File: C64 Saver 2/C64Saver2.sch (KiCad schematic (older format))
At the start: 20 parts, among them J1 Conn_01x04, J2 Conn_01x08, J4 Conn_01x08, J5 Conn_01x04, J6 Conn_01x04, Q1 2N7002, Q2 Q_PMOS_GDS

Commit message: resistor values
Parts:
- R1, R6: value R -> 3k9
- R2, R3: value R -> 3k3
- R4: value R -> 330k
- R5: value R -> 33k
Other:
- moved on the sheet: R1, R3
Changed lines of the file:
@@
 L R R1
 U 1 1 5AFB3CB5
-P 3650 3050
-F 0 "R1" V 3730 3050 50  0000 C CNN
-F 1 "R" V 3650 3050 50  0000 C CNN
-F 2 "Resistors_THT:R_Axial_DIN0204_L3.6mm_D1.6mm_P5.08mm_Horizontal" V 3580 3050 50  0001 C CNN
-F 3 "" H 3650 3050 50  0001 C CNN
-	1    3650 3050
+P 3650 3150
+F 0 "R1" V 3730 3150 50  0000 C CNN
+F 1 "3k9" V 3650 3150 50  0000 C CNN
+F 2 "Resistors_THT:R_Axial_DIN0204_L3.6mm_D1.6mm_P5.08mm_Horizontal" V 3580 3150 50  0001 C CNN
+F 3 "" H 3650 3150 50  0001 C CNN
+	1    3650 3150
 	1    0    0    -1
 $EndComp
@@
 P 3650 4300
 F 0 "R2" V 3730 4300 50  0000 C CNN
-F 1 "R" V 3650 4300 50  0000 C CNN
+F 1 "3k3" V 3650 4300 50  0000 C CNN
 F 2 "Resistors_THT:R_Axial_DIN0204_L3.6mm_D1.6mm_P5.08mm_Horizontal" V 3580 4300 50  0001 C CNN
 F 3 "" H 3650 4300 50  0001 C CNN
@@
 L R R3
 U 1 1 5B1D6DA9
-P 4050 3050
-F 0 "R3" V 4130 3050 50  0000 C CNN
-F 1 "R" V 4050 3050 50  0000 C CNN
-F 2 "Resistors_THT:R_Axial_DIN0204_L3.6mm_D1.6mm_P5.08mm_Horizontal" V 3980 3050 50  0001 C CNN
-F 3 "" H 4050 3050 50  0001 C CNN
-	1    4050 3050
+P 4050 3150
+F 0 "R3" V 4130 3150 50  0000 C CNN
+F 1 "3k3" V 4050 3150 50  0000 C CNN
+F 2 "Resistors_THT:R_Axial_DIN0204_L3.6mm_D1.6mm_P5.08mm_Horizontal" V 3980 3150 50  0001 C CNN
+F 3 "" H 4050 3150 50  0001 C CNN
+	1    4050 3150
 	1    0    0    -1
 $EndComp
@@
 P 5300 3450
 F 0 "R6" V 5380 3450 50  0000 C CNN
-F 1 "R" V 5300 3450 50  0000 C CNN
+F 1 "3k9" V 5300 3450 50  0000 C CNN
 F 2 "Resistors_THT:R_Axial_DIN0204_L3.6mm_D1.6mm_P5.08mm_Horizontal" V 5230 3450 50  0001 C CNN
 F 3 "" H 5300 3450 50  0001 C CNN
@@
 P 4700 2950
 F 0 "R5" V 4780 2950 50  0000 C CNN
-F 1 "R" V 4700 2950 50  0000 C CNN
+F 1 "33k" V 4700 2950 50  0000 C CNN
 F 2 "Resistors_THT:R_Axial_DIN0204_L3.6mm_D1.6mm_P5.08mm_Horizontal" V 4630 2950 50  0001 C CNN
 F 3 "" H 4700 2950 50  0001 C CNN
@@
 P 4550 3650
 F 0 "R4" V 4630 3650 50  0000 C CNN
-F 1 "R" V 4550 3650 50  0000 C CNN
+F 1 "330k" V 4550 3650 50  0000 C CNN
 F 2 "Resistors_THT:R_Axial_DIN0204_L3.6mm_D1.6mm_P5.08mm_Horizontal" V 4480 3650 50  0001 C CNN
 F 3 "" H 4550 3650 50  0001 C CNN
@@
 	3650 4100 3950 4100
 Wire Wire Line
-	3650 3200 3650 4150
+	3650 3300 3650 3650
+Wire Wire Line
+	3650 3650 3650 4100
+Wire Wire Line
+	3650 4100 3650 4150
 Connection ~ 3650 4100
 Wire Wire Line
 	4050 4500 4050 4200
 Wire Wire Line
-	2050 4500 7800 4500
+	2050 4500 2550 4500
+Wire Wire Line
+	2550 4500 3150 4500
+Wire Wire Line
+	3150 4500 3650 4500
+Wire Wire Line
+	3650 4500 4050 4500
+Wire Wire Line
+	4050 4500 4500 4500
+Wire Wire Line
+	4500 4500 4900 4500
+Wire Wire Line
+	4900 4500 5300 4500
+Wire Wire Line
+	5300 4500 7800 4500
 Wire Wire Line
 	3650 4500 3650 4450
 Wire Wire Line
-	4050 3200 4050 4000
-Wire Wire Line
-	4050 2700 4050 2900
-Wire Wire Line
-	3650 2700 3650 2900
+	4050 3300 4050 3900
+Wire Wire Line
+	4050 3900 4050 4000
+Wire Wire Line
+	4050 2700 4050 3000
+Wire Wire Line
+	3650 2700 3650 3000
 Connection ~ 3650 2700
 Wire Wire Line
 	4500 4050 4500 3900
 Wire Wire Line
-	4050 3900 5000 3900
+	4050 3900 4500 3900
+Wire Wire Line
+	4500 3900 4900 3900
+Wire Wire Line
+	4900 3900 5000 3900
 Connection ~ 4050 3900
 Wire Wire Line
@@
 Connection ~ 4900 4500
 Wire Wire Line
-	5300 3600 5300 3700
+	5300 3600 5300 3650
+Wire Wire Line
+	5300 3650 5300 3700
 Connection ~ 4050 2700
 Connection ~ 5000 2700
@@
 	4700 3100 4700 3200
 Wire Wire Line
-	4700 3200 5450 3200
+	4700 3200 5000 3200
+Wire Wire Line
+	5000 3200 5300 3200
+Wire Wire Line
+	5300 3200 5450 3200
 Connection ~ 5300 3200
 Connection ~ 5000 3200
 Wire Wire Line
-	4700 3650 5400 3650
+	4700 3650 5300 3650
+Wire Wire Line
+	5300 3650 5400 3650
 Connection ~ 5300 3650
 Wire Wire Line
@@
 	1700 3650 1800 3650
 Wire Wire Line
-	3000 2700 5100 2700
+	3000 2700 3150 2700
+Wire Wire Line
+	3150 2700 3650 2700
+Wire Wire Line
+	3650 2700 4050 2700
+Wire Wire Line
+	4050 2700 4700 2700
+Wire Wire Line
+	4700 2700 5000 2700
+Wire Wire Line
+	5000 2700 5100 2700
 Wire Wire Line
 	1800 2700 2500 2700
@@
 Connection ~ 2550 4500
 Wire Wire Line
-	5300 3000 5300 3300
+	5300 3000 5300 3200
+Wire Wire Line
+	5300 3200 5300 3300
 Wire Wire Line
 	5500 2700 7800 2700
@@
 $EndComp
 Wire Wire Line
-	2500 2700 2500 1850
-Wire Wire Line
-	3000 2700 3000 1850
+	2500 2700 2500 1950
+Wire Wire Line
+	2500 1950 2500 1850
+Wire Wire Line
+	3000 2700 3000 1950
+Wire Wire Line
+	3000 1950 3000 1850
 Wire Wire Line
 	2400 1850 2400 1950
 Wire Wire Line
-	2400 1950 2700 1950
+	2400 1950 2500 1950
+Wire Wire Line
+	2500 1950 2600 1950
+Wire Wire Line
+	2600 1950 2700 1950
 Connection ~ 2500 1950
 Wire Wire Line
@@
 	2900 1850 2900 1950
 Wire Wire Line
-	2800 1950 3100 1950
+	2800 1950 2900 1950
+Wire Wire Line
+	2900 1950 3000 1950
+Wire Wire Line
+	3000 1950 3100 1950
 Connection ~ 3000 1950
 Wire Wire Line
@@
 	3500 5400 3500 5500
 Wire Wire Line
-	3200 5400 3500 5400
+	3200 5400 3300 5400
+Wire Wire Line
+	3300 5400 3400 5400
+Wire Wire Line
+	3400 5400 3500 5400
 Connection ~ 3400 5400
 Wire Wire Line
@@
 	3700 5500 3700 5400
 Wire Wire Line
-	3600 5400 3900 5400
+	3600 5400 3700 5400
+Wire Wire Line
+	3700 5400 3800 5400
+Wire Wire Line
+	3800 5400 3900 5400
 Connection ~ 3600 5400
 Wire Wire Line
@@
 	3600 4900 8050 4900
 Wire Wire Line
-	1900 4800 7950 4800
-Wire Wire Line
-	3400 4900 3400 5500
-Wire Wire Line
-	3600 4900 3600 5500
+	1900 4800 4250 4800
+Wire Wire Line
+	4250 4800 7950 4800
+Wire Wire Line
+	3400 4900 3400 5400
+Wire Wire Line
+	3400 5400 3400 5500
+Wire Wire Line
+	3600 4900 3600 5400
+Wire Wire Line
+	3600 5400 3600 5500
 Connection ~ 4250 4800
 $EndSCHEMATC

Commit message: date and version
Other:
- note added: "2.2"
- note added: "2018-08-09"
- note removed: "2.1"
- note removed: "2018-07-23"
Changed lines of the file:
@@
 $EndComp
 Text Notes 10600 7650 0    60   ~ 0
-2.1
+2.2
 Text Notes 7400 7500 0    79   ~ 0
 C64 Saver
 Text Notes 8200 7650 0    79   ~ 0
-2018-07-23
+2018-08-09
 Text Label 3050 4900 0    49   ~ 0
 9VAC1

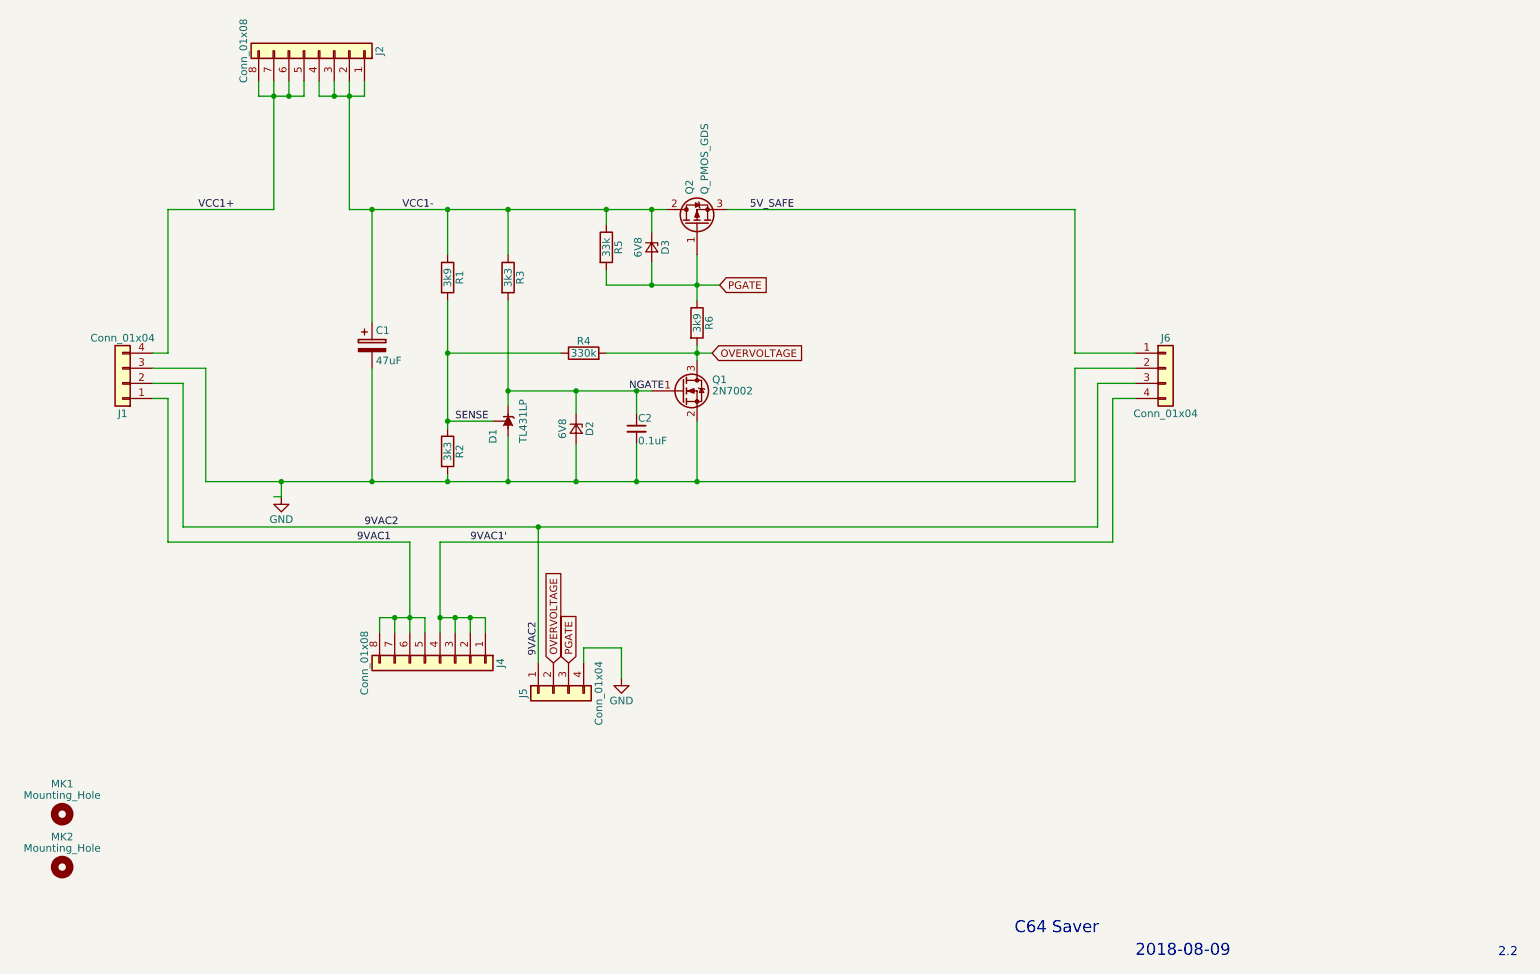
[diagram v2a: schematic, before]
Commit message: release saver v2.2
got fix for rotated resistor
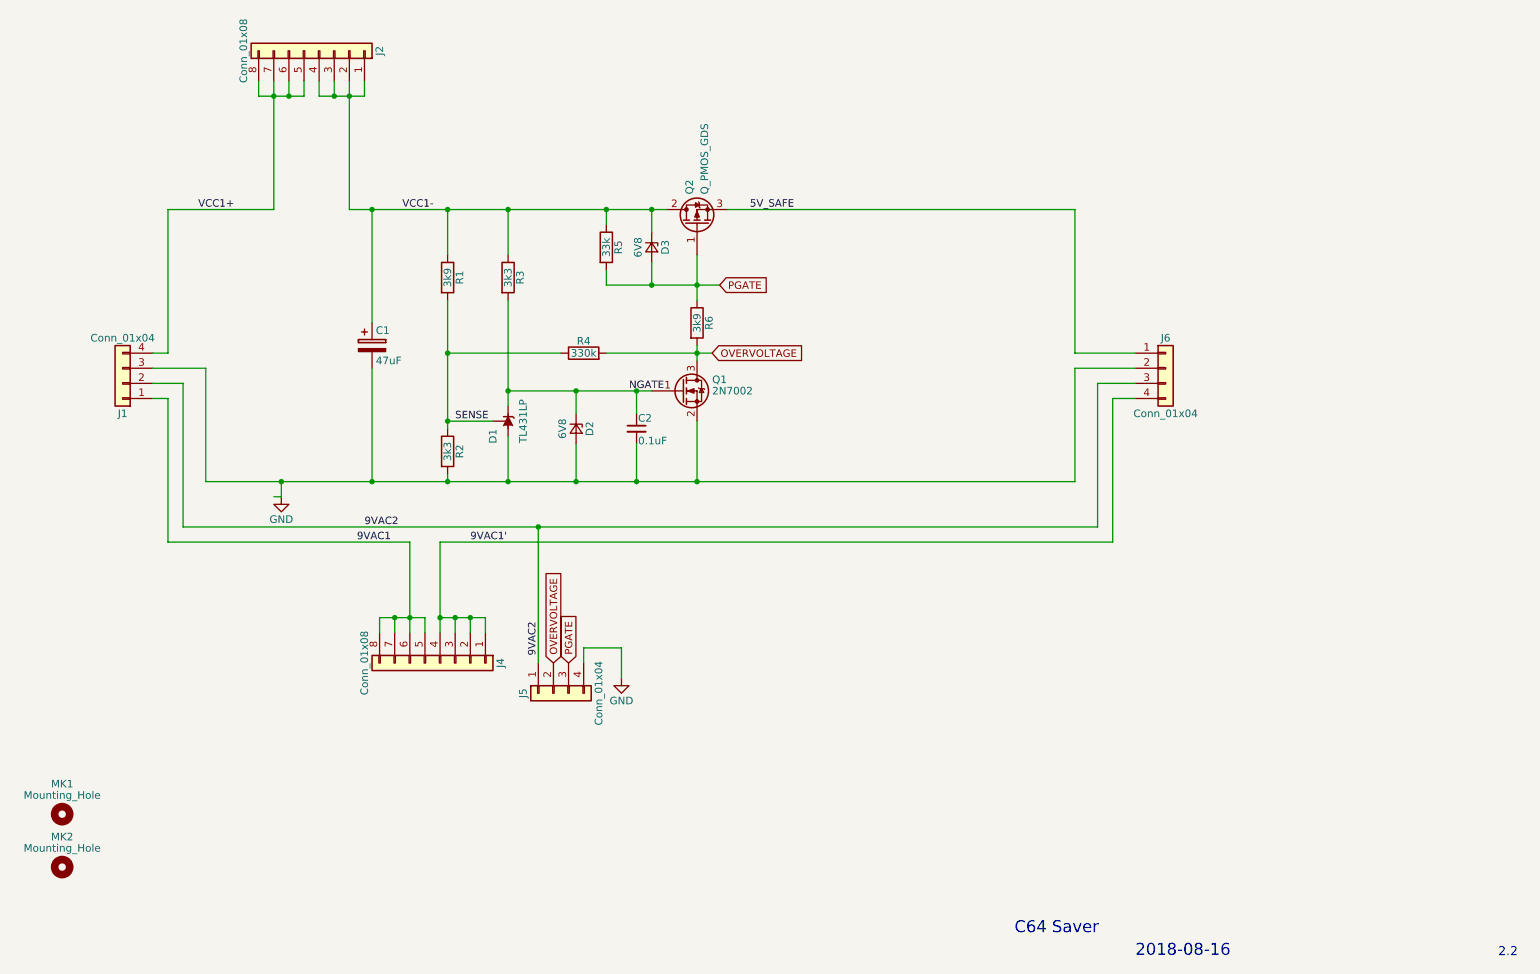
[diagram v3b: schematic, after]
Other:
- note added: "2018-08-16"
- note removed: "2018-08-09"
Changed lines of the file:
@@
 C64 Saver
 Text Notes 8200 7650 0    79   ~ 0
-2018-08-09
+2018-08-16
 Text Label 3050 4900 0    49   ~ 0
 9VAC1
@@
 	3650 4100 3950 4100
 Wire Wire Line
-	3650 3300 3650 3650
-Wire Wire Line
-	3650 3650 3650 4100
-Wire Wire Line
-	3650 4100 3650 4150
+	3650 3300 3650 4150
 Connection ~ 3650 4100
 Wire Wire Line
 	4050 4500 4050 4200
 Wire Wire Line
-	2050 4500 2550 4500
-Wire Wire Line
-	2550 4500 3150 4500
-Wire Wire Line
-	3150 4500 3650 4500
-Wire Wire Line
-	3650 4500 4050 4500
-Wire Wire Line
-	4050 4500 4500 4500
-Wire Wire Line
-	4500 4500 4900 4500
-Wire Wire Line
-	4900 4500 5300 4500
-Wire Wire Line
-	5300 4500 7800 4500
+	2050 4500 7800 4500
 Wire Wire Line
 	3650 4500 3650 4450
 Wire Wire Line
-	4050 3300 4050 3900
-Wire Wire Line
-	4050 3900 4050 4000
+	4050 3300 4050 4000
 Wire Wire Line
 	4050 2700 4050 3000
@@
 	4500 4050 4500 3900
 Wire Wire Line
-	4050 3900 4500 3900
-Wire Wire Line
-	4500 3900 4900 3900
-Wire Wire Line
-	4900 3900 5000 3900
+	4050 3900 5000 3900
 Connection ~ 4050 3900
 Wire Wire Line
@@
 Connection ~ 4900 4500
 Wire Wire Line
-	5300 3600 5300 3650
-Wire Wire Line
-	5300 3650 5300 3700
+	5300 3600 5300 3700
 Connection ~ 4050 2700
 Connection ~ 5000 2700
@@
 	4700 3100 4700 3200
 Wire Wire Line
-	4700 3200 5000 3200
-Wire Wire Line
-	5000 3200 5300 3200
-Wire Wire Line
-	5300 3200 5450 3200
+	4700 3200 5450 3200
 Connection ~ 5300 3200
 Connection ~ 5000 3200
 Wire Wire Line
-	4700 3650 5300 3650
-Wire Wire Line
-	5300 3650 5400 3650
+	4700 3650 5400 3650
 Connection ~ 5300 3650
 Wire Wire Line
@@
 	1700 3650 1800 3650
 Wire Wire Line
-	3000 2700 3150 2700
-Wire Wire Line
-	3150 2700 3650 2700
-Wire Wire Line
-	3650 2700 4050 2700
-Wire Wire Line
-	4050 2700 4700 2700
-Wire Wire Line
-	4700 2700 5000 2700
-Wire Wire Line
-	5000 2700 5100 2700
+	3000 2700 5100 2700
 Wire Wire Line
 	1800 2700 2500 2700
@@
 Connection ~ 2550 4500
 Wire Wire Line
-	5300 3000 5300 3200
-Wire Wire Line
-	5300 3200 5300 3300
+	5300 3000 5300 3300
 Wire Wire Line
 	5500 2700 7800 2700
@@
 $EndComp
 Wire Wire Line
-	2500 2700 2500 1950
-Wire Wire Line
-	2500 1950 2500 1850
-Wire Wire Line
-	3000 2700 3000 1950
-Wire Wire Line
-	3000 1950 3000 1850
+	2500 2700 2500 1850
+Wire Wire Line
+	3000 1850 3000 2700
 Wire Wire Line
 	2400 1850 2400 1950
 Wire Wire Line
-	2400 1950 2500 1950
-Wire Wire Line
-	2500 1950 2600 1950
-Wire Wire Line
-	2600 1950 2700 1950
+	2400 1950 2700 1950
 Connection ~ 2500 1950
 Wire Wire Line
@@
 	2900 1850 2900 1950
 Wire Wire Line
-	2800 1950 2900 1950
-Wire Wire Line
-	2900 1950 3000 1950
-Wire Wire Line
-	3000 1950 3100 1950
+	2800 1950 3100 1950
 Connection ~ 3000 1950
 Wire Wire Line
@@
 	3500 5400 3500 5500
 Wire Wire Line
-	3200 5400 3300 5400
-Wire Wire Line
-	3300 5400 3400 5400
-Wire Wire Line
-	3400 5400 3500 5400
+	3200 5400 3500 5400
 Connection ~ 3400 5400
 Wire Wire Line
@@
 	3700 5500 3700 5400
 Wire Wire Line
-	3600 5400 3700 5400
-Wire Wire Line
-	3700 5400 3800 5400
-Wire Wire Line
-	3800 5400 3900 5400
+	3600 5400 3900 5400
 Connection ~ 3600 5400
 Wire Wire Line
@@
 	3600 4900 8050 4900
 Wire Wire Line
-	1900 4800 4250 4800
-Wire Wire Line
-	4250 4800 7950 4800
-Wire Wire Line
-	3400 4900 3400 5400
-Wire Wire Line
-	3400 5400 3400 5500
-Wire Wire Line
-	3600 4900 3600 5400
-Wire Wire Line
-	3600 5400 3600 5500
+	1900 4800 7950 4800
+Wire Wire Line
+	3400 4900 3400 5500
+Wire Wire Line
+	3600 4900 3600 5500
 Connection ~ 4250 4800
 $EndSCHEMATC

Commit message: v2.3
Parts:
- removed Q1: 2N7002, TO_SOT_Packages_THT:TO-92_Molded_Narrow, symbol 2N7002
- added Q1: 2N7000, TO_SOT_Packages_THT:TO-92_Molded_Narrow, symbol 2N7000
- Q2: value Q_PMOS_GDS -> IRFR5305
- R5: value 33k -> 3k3
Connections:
- net 5V_SAFE: now also Q2.2 (D); no longer Q2.3 (S)
- net GND: now also Q1.1 (S)
- net NGATE: now also Q1.2 (G)
- net OVERVOLTAGE: now also R5.2, Q1.3 (D)
- net PGATE: no longer R5.2
- net VCC1-: now also Q2.3 (S); no longer Q2.2 (D)
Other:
- note added: "2.3"
- note added: "2018-08-18"
- note removed: "2.2"
- note removed: "2018-08-16"
- moved on the sheet: D3, R4, R6
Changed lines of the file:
@@
-$EndComp
-$Comp
-L 2N7002 Q1
-U 1 1 5B1D3AF8
-P 5200 3900
-F 0 "Q1" H 5400 3975 50  0000 L CNN
-F 1 "2N7002" H 5400 3900 50  0000 L CNN
-F 2 "TO_SOT_Packages_THT:TO-92_Molded_Narrow" H 5400 3825 50  0001 L CIN
-F 3 "" H 5200 3900 50  0001 L CNN
-	1    5200 3900
-	1    0    0    -1
 $EndComp
 $Comp
@@
 L R R6
 U 1 1 5B1D73D7
-P 5300 3450
-F 0 "R6" V 5380 3450 50  0000 C CNN
-F 1 "3k9" V 5300 3450 50  0000 C CNN
-F 2 "Resistors_THT:R_Axial_DIN0204_L3.6mm_D1.6mm_P5.08mm_Horizontal" V 5230 3450 50  0001 C CNN
-F 3 "" H 5300 3450 50  0001 C CNN
-	1    5300 3450
+P 5300 3350
+F 0 "R6" V 5380 3350 50  0000 C CNN
+F 1 "3k9" V 5300 3350 50  0000 C CNN
+F 2 "Resistors_THT:R_Axial_DIN0204_L3.6mm_D1.6mm_P5.08mm_Horizontal" V 5230 3350 50  0001 C CNN
+F 3 "" H 5300 3350 50  0001 C CNN
+	1    5300 3350
 	1    0    0    -1
 $EndComp
@@
 P 4700 2950
 F 0 "R5" V 4780 2950 50  0000 C CNN
-F 1 "33k" V 4700 2950 50  0000 C CNN
+F 1 "3k3" V 4700 2950 50  0000 C CNN
 F 2 "Resistors_THT:R_Axial_DIN0204_L3.6mm_D1.6mm_P5.08mm_Horizontal" V 4630 2950 50  0001 C CNN
 F 3 "" H 4700 2950 50  0001 C CNN
@@
 L D_Zener_Small D3
 U 1 1 5B1D7545
-P 5000 2950
-F 0 "D3" H 5000 3040 50  0000 C CNN
-F 1 "6V8" H 5000 2860 50  0000 C CNN
-F 2 "Diodes_THT:D_DO-35_SOD27_P7.62mm_Horizontal" V 5000 2950 50  0001 C CNN
-F 3 "" V 5000 2950 50  0001 C CNN
-	1    5000 2950
+P 5000 2900
+F 0 "D3" H 5000 2990 50  0000 C CNN
+F 1 "6V8" H 5000 2810 50  0000 C CNN
+F 2 "Diodes_THT:D_DO-35_SOD27_P7.62mm_Horizontal" V 5000 2900 50  0001 C CNN
+F 3 "" V 5000 2900 50  0001 C CNN
+	1    5000 2900
 	0    1    1    0
 $EndComp
@@
 L R R4
 U 1 1 5B1D9590
-P 4550 3650
-F 0 "R4" V 4630 3650 50  0000 C CNN
-F 1 "330k" V 4550 3650 50  0000 C CNN
-F 2 "Resistors_THT:R_Axial_DIN0204_L3.6mm_D1.6mm_P5.08mm_Horizontal" V 4480 3650 50  0001 C CNN
-F 3 "" H 4550 3650 50  0001 C CNN
-	1    4550 3650
+P 4300 3650
+F 0 "R4" V 4380 3650 50  0000 C CNN
+F 1 "330k" V 4300 3650 50  0000 C CNN
+F 2 "Resistors_THT:R_Axial_DIN0204_L3.6mm_D1.6mm_P5.08mm_Horizontal" V 4230 3650 50  0001 C CNN
+F 3 "" H 4300 3650 50  0001 C CNN
+	1    4300 3650
 	0    -1   -1   0
 $EndComp
-Text GLabel 5450 3200 2    49   Input ~ 0
+Text GLabel 5400 3100 2    49   Input ~ 0
 PGATE
 Text Label 3800 4900 0    49   ~ 0
@@
 U 1 1 5B217093
 P 5300 2800
-F 0 "Q2" H 5500 2850 50  0000 L CNN
-F 1 "Q_PMOS_GDS" H 5500 2750 50  0000 L CNN
+F 0 "Q2" V 5500 2850 50  0000 L CNN
+F 1 "IRFR5305" V 5600 2850 50  0000 L CNN
 F 2 "TO_SOT_Packages_SMD:ATPAK-2" H 5500 2900 50  0001 C CNN
 F 3 "" H 5300 2800 50  0001 C CNN
 	1    5300 2800
-	0    -1   -1   0
+	0    1    -1   0
 $EndComp
 Text Notes 10600 7650 0    60   ~ 0
-2.2
+2.3
 Text Notes 7400 7500 0    79   ~ 0
 C64 Saver
 Text Notes 8200 7650 0    79   ~ 0
-2018-08-16
+2018-08-18
 Text Label 3050 4900 0    49   ~ 0
 9VAC1
@@
 Connection ~ 4900 4500
 Wire Wire Line
-	5300 3600 5300 3700
+	5300 3500 5300 3700
 Connection ~ 4050 2700
 Connection ~ 5000 2700
 Wire Wire Line
-	5000 3050 5000 3200
+	5000 3000 5000 3100
 Wire Wire Line
 	4700 2700 4700 2800
 Connection ~ 4700 2700
 Wire Wire Line
-	4700 3100 4700 3200
-Wire Wire Line
-	4700 3200 5450 3200
-Connection ~ 5300 3200
-Connection ~ 5000 3200
-Wire Wire Line
-	4700 3650 5400 3650
+	4700 3100 4700 3650
+Connection ~ 5300 3100
+Wire Wire Line
+	4450 3650 5400 3650
 Connection ~ 5300 3650
 Wire Wire Line
-	4400 3650 3650 3650
+	4150 3650 3650 3650
 Connection ~ 3650 3650
 Connection ~ 3650 4500
@@
 Connection ~ 2550 4500
 Wire Wire Line
-	5300 3000 5300 3300
+	5300 3000 5300 3200
 Wire Wire Line
 	5500 2700 7800 2700
 Wire Wire Line
-	5000 2850 5000 2700
+	5000 2800 5000 2700
 Wire Wire Line
 	3150 3450 3150 2700
@@
 	3600 4900 3600 5500
 Connection ~ 4250 4800
+Wire Wire Line
+	5000 3100 5400 3100
+Connection ~ 4700 3650
+$Comp
+L 2N7000 Q1
+U 1 1 5B78C547
+P 5200 3900
+F 0 "Q1" H 5400 3975 50  0000 L CNN
+F 1 "2N7000" H 5400 3900 50  0000 L CNN
+F 2 "TO_SOT_Packages_THT:TO-92_Molded_Narrow" H 5400 3825 50  0001 L CIN
+F 3 "" H 5200 3900 50  0001 L CNN
+	1    5200 3900
+	1    0    0    -1
+$EndComp
 $EndSCHEMATC
